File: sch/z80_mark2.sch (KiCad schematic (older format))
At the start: 0 parts

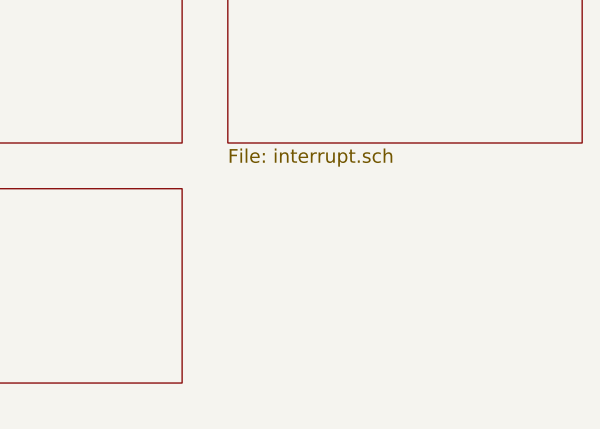
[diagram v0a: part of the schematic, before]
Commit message: Added new schematics and about to start coding for new MMU.
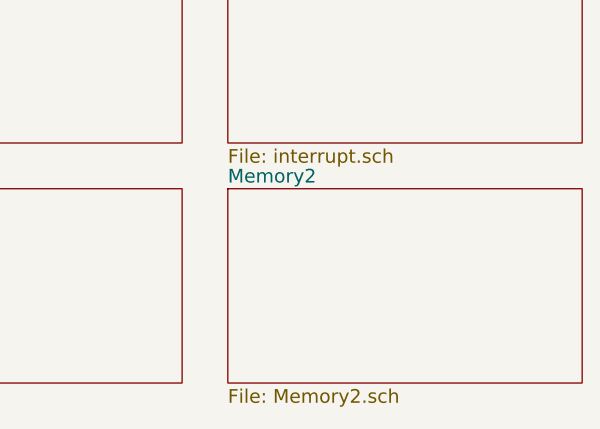
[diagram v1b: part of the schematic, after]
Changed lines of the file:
@@
-EESchema Schematic File Version 2  date Fri 17 Dec 2010 20:03:20 GMT
+EESchema Schematic File Version 2  date Sat 19 Feb 2011 16:33:30 GMT
 LIBS:74xx
 LIBS:adc-dac
@@
 EELAYER END
 $Descr A4 11700 8267
-Sheet 1 12
+Sheet 1 13
 Title "noname.sch"
-Date "17 dec 2010"
+Date "19 feb 2011"
 Rev ""
 Comp ""
@@
 $EndDescr
 $Sheet
+S 6950 3850 1550 850
+U 4D4F0F7A
+F0 "Memory2" 60
+F1 "Memory2.sch" 60
+$EndSheet
+$Sheet
 S 5200 3850 1550 850
